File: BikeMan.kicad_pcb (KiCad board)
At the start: 2 copper layers, 152.4 x 127 mm, 86 parts, among them J1 USB_A_stacked, J10 Conn_01x04_Female, J11 Conn_01x04_Female, J12 MagJack, J13 Micro_SD_Card_Det, J14 HDMI_A_1.4, J2 USB_A_stacked, J3 Barrel_Jack, J4 Conn_01x06_Female, J5 Conn_01x06_Female, J6 Conn_01x06_Female, J7 PushConnector_8pos, J8 PushConnector_8pos, J9 PushConnector_8pos, Q1 AUIRF7316QTR, Q2 AUIRF7316QTR, Q3 AUIRF7316QTR, Q4 AUIRF7316QTR, Q5 DMN62D0U-7, Q6 DMN62D0U-7, U1 RT9742GGJ5, U2 TUSB2046IBVF, U3 AP64501, U4 MCP2515, U5 MCP2551, U6 NPIC6C596ADJ, U7 PCF8574DWR, U8 PCF85063A

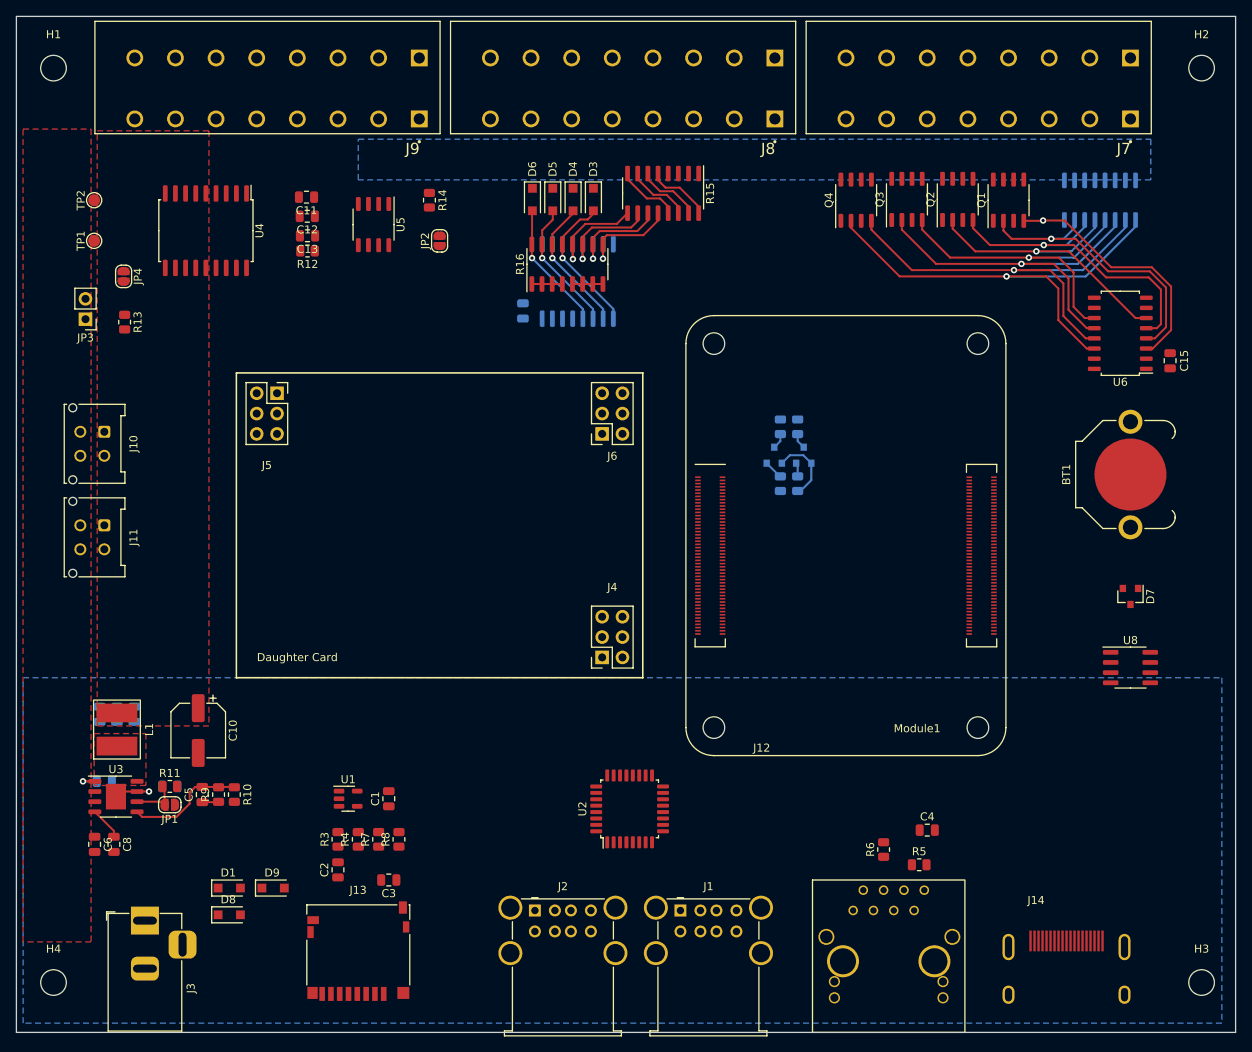
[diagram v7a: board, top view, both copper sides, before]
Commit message: Routing for HDMI, Ethernet, SD Card, CAN
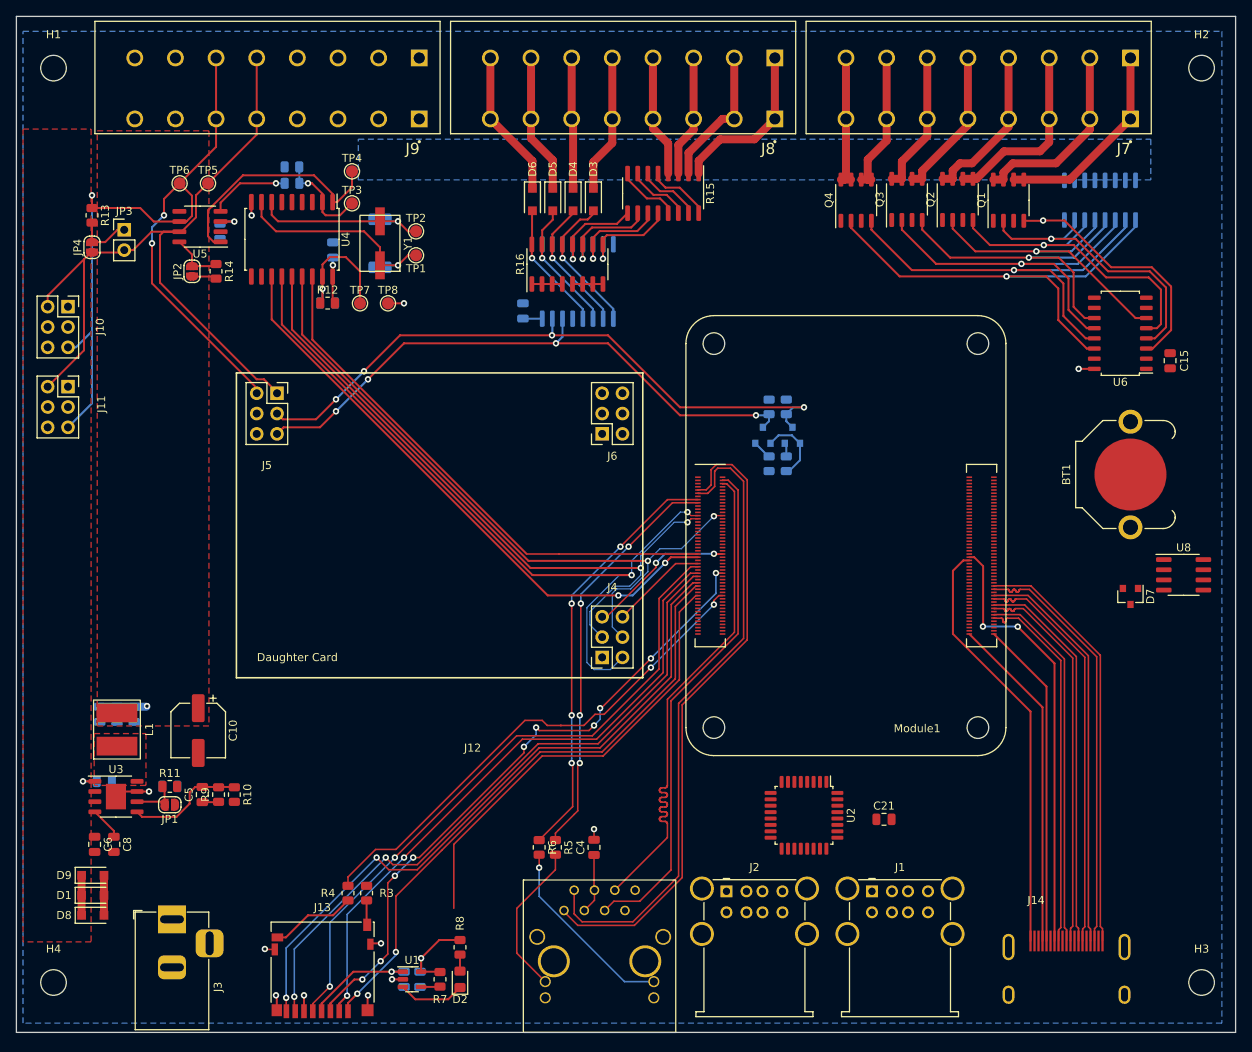
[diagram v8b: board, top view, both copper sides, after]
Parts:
- removed C3: C, Capacitor_SMD:C_0805_2012Metric
- added C19: C, Capacitor_SMD:C_0805_2012Metric, B.Cu at (94.6, 60.8)
- added C20: C, Capacitor_SMD:C_0805_2012Metric, B.Cu at (80.5, 58.5)
- added C21: 0.1uF, Capacitor_SMD:C_0805_2012Metric, F.Cu at (163.5, 132.0)
- added D2: LED_Red, LED_SMD:LED_0805_2012Metric_Pad1.15x1.40mm_HandSolder, F.Cu at (110.5, 152.0)
- added R20: 10k, Resistor_SMD:R_0805_2012Metric, B.Cu at (89.5, 52.5)
- added R21: 22k, Resistor_SMD:R_0805_2012Metric, B.Cu at (89.5, 50.4)
- added TP3: TestPoint, TestPoint:TestPoint_Pad_D1.5mm, F.Cu at (97.0, 55.0)
- added TP4: TestPoint, TestPoint:TestPoint_Pad_D1.5mm, F.Cu at (97.0, 51.0)
- added TP5: TestPoint, TestPoint:TestPoint_Pad_D1.5mm, F.Cu at (79.0, 52.5)
- added TP6: TestPoint, TestPoint:TestPoint_Pad_D1.5mm, F.Cu at (75.5, 52.5)
- added TP7: TestPoint, TestPoint:TestPoint_Pad_D1.5mm, F.Cu at (98.0, 67.5)
- added TP8: TestPoint, TestPoint:TestPoint_Pad_D1.5mm, F.Cu at (101.5, 67.5)
- added Y1: ABLS7M-16.000MHZ-B-2-T, footprints:Crystal-ABLS7M, F.Cu at (100.5, 60.0)
- C1, C11, C12, C13, C2: moved to B.Cu
- J10, J11: value Conn_01x04_Female -> Conn_01x06_Male; footprint Connector_Molex:Molex_Micro-Fit_3.0_43045-0412_2x02_P3.00mm_Vertical -> Connector_PinSocket_2.54mm:PinSocket_2x03_P2.54mm_Vertical
- moved R5 45.5 mm to (122.4, 135.5), turned to -90 degrees
- moved R6 43.1 mm to (120.4, 135.5), turned to -90 degrees
- moved C4 41.7 mm to (127.3, 135.5), turned to 90 degrees
- moved TP2 40.4 mm to (105.0, 58.5), turned to 0 degrees
- moved TP1 40.3 mm to (105.0, 61.5), turned to 0 degrees
- moved J12 36.1 mm to (123.5, 143.4)
- moved JP2 31.2 mm to (77.0, 63.5)
- moved R14 28.1 mm to (80.0, 63.5)
- moved J2 24.1 mm to (143.8, 141.0)
- moved J1 24.1 mm to (162.0, 141.0)
- moved U1 23.9 mm to (104.5, 152.0)
- moved C1 22.9 mm to (105.5, 152.0), turned to -90 degrees
- moved D9 22.6 mm to (64.6, 139.0)
- moved U2 21.8 mm to (153.5, 131.5), turned to -90 degrees
- moved U5 21.7 mm to (78.0, 57.9), turned to 180 degrees
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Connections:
- net /ComputeModule_A/Eth_Rx_{+} renamed /ComputeModule_A/Eth_Rx+
- net /ComputeModule_A/Eth_Rx_{-} renamed /ComputeModule_A/Eth_Rx-
- net /ComputeModule_A/Eth_Tx_{+} renamed /ComputeModule_A/Eth_Tx+
- net /ComputeModule_A/Eth_Tx_{-} renamed /ComputeModule_A/Eth_Tx-
- H1 pad 1: no_connect_209 -> no_connect_211
- H2 pad 1: no_connect_210 -> no_connect_212
- H3 pad 1: no_connect_211 -> no_connect_213
- H4 pad 1: no_connect_212 -> no_connect_214
- J1 pad 3: /D_{2}+ -> /D_{2}-
- J1 pad 6: /D_{1}+ -> /D_{1}-
- J10 pad 3: /CAN_{L} -> +12V
- J11 pad 3: /CAN_{L} -> +12V
- J12 pad 1: no_connect_213 -> no_connect_215
- J12 pad 8: no_connect_215 -> no_connect_217
- J13 pad 4: /ComputeModule_A/SD.power -> /ComputeModule_A/SD.POWER
- J2 pad 2: /D_{4}+ -> /D_{4}-
- J2 pad 6: /D_{3}+ -> /D_{3}-
- J4 pad 2: /CAN_{H} -> /SPI.CLK
- J4 pad 3: /CAN_{L} -> /SPI.MOSI
- J4 pad 4: /SDA_{5V} -> /SPI.MISO
- J4 pad 5: /SCL_{5V} -> /SPI.~CS_{ES1}
- J4 pad 6: GND -> /~INT_{ES1}
- J5 pad 1: +12V -> /CAN_{H}
- J5 pad 2: /SPI.MISO -> /CAN_{L}
- J5 pad 3: /SPI.MOSI -> /SDA_{5V}
- J5 pad 4: /SPI.CLK -> +12V
- J5 pad 5: /SPI.~CS_{ES1} -> /SCL_{5V}
- J5 pad 6: /~INT_{ES1} -> GND
- J9 pad 1: +12V -> GND
- J9 pad 2: +12V -> GND
- J9 pad 3: /CAN_{H} -> GND
- J9 pad 4: /CAN_{L} -> GND
- J9 pad 5: GND -> /CAN_{H}
- J9 pad 6: GND -> /CAN_{L}
- J9 pad 7: GND -> +12V
- J9 pad 8: GND -> +12V
- Module1 pad 10: no_connect_216 -> no_connect_218
- Module1 pad 102: no_connect_217 -> no_connect_219
- Module1 pad 104: no_connect_218 -> no_connect_220
- Module1 pad 106: no_connect_219 -> no_connect_221
- Module1 pad 109: no_connect_220 -> no_connect_222
- Module1 pad 110: no_connect_221 -> no_connect_223
- Module1 pad 111: no_connect_222 -> no_connect_224
- Module1 pad 112: no_connect_223 -> no_connect_225
- Module1 pad 115: no_connect_224 -> no_connect_226
- Module1 pad 116: no_connect_225 -> no_connect_227
- Module1 pad 117: no_connect_226 -> no_connect_228
- Module1 pad 118: no_connect_227 -> no_connect_229
- Module1 pad 12: no_connect_228 -> no_connect_230
- Module1 pad 121: no_connect_229 -> no_connect_231
- Module1 pad 122: no_connect_230 -> no_connect_232
- Module1 pad 123: no_connect_231 -> no_connect_233
- Module1 pad 124: no_connect_232 -> no_connect_234
- Module1 pad 127: no_connect_233 -> no_connect_235
- Module1 pad 128: no_connect_234 -> no_connect_236
- Module1 pad 129: no_connect_235 -> no_connect_237
- Module1 pad 130: no_connect_236 -> no_connect_238
- Module1 pad 133: no_connect_237 -> no_connect_239
- Module1 pad 134: no_connect_238 -> no_connect_240
- Module1 pad 135: no_connect_239 -> no_connect_241
- Module1 pad 136: no_connect_240 -> no_connect_242
- Module1 pad 139: no_connect_241 -> no_connect_243
- Module1 pad 140: no_connect_242 -> no_connect_244
- Module1 pad 141: no_connect_243 -> no_connect_245
- Module1 pad 142: no_connect_244 -> no_connect_246
- Module1 pad 143: no_connect_245 -> no_connect_247
- Module1 pad 145: no_connect_246 -> no_connect_248
- Module1 pad 146: no_connect_247 -> no_connect_249
- Module1 pad 147: no_connect_248 -> no_connect_250
- Module1 pad 148: no_connect_249 -> no_connect_251
- Module1 pad 149: no_connect_250 -> no_connect_252
- Module1 pad 152: no_connect_251 -> no_connect_253
- Module1 pad 154: no_connect_252 -> no_connect_254
- Module1 pad 157: no_connect_253 -> no_connect_255
- Module1 pad 158: no_connect_254 -> no_connect_256
- Module1 pad 159: no_connect_255 -> no_connect_257
- Module1 pad 160: no_connect_256 -> no_connect_258
- Module1 pad 163: no_connect_257 -> no_connect_259
- Module1 pad 164: no_connect_258 -> no_connect_260
- Module1 pad 165: no_connect_259 -> no_connect_261
- Module1 pad 166: no_connect_260 -> no_connect_262
- Module1 pad 169: no_connect_261 -> no_connect_263
- Module1 pad 171: no_connect_262 -> no_connect_264
- Module1 pad 175: no_connect_263 -> no_connect_265
- Module1 pad 177: no_connect_264 -> no_connect_266
- Module1 pad 181: no_connect_265 -> no_connect_267
- Module1 pad 183: no_connect_266 -> no_connect_268
- Module1 pad 187: no_connect_267 -> no_connect_269
- Module1 pad 189: no_connect_268 -> no_connect_270
- Module1 pad 19: no_connect_269 -> no_connect_271
- Module1 pad 193: no_connect_270 -> no_connect_272
- Module1 pad 195: no_connect_271 -> no_connect_273
- Module1 pad 25: /~GPIO_{OE} -> /SPI.CLK
- Module1 pad 26: Net-(Module1-Pad26) -> /SPI.MISO
- Module1 pad 27: /~GPIO_{RS} -> /SPI.MOSI
- Module1 pad 29: /GPIO_{rCLK} -> Net-(Module1-Pad29)
- Module1 pad 3: no_connect_272 -> no_connect_274
- Module1 pad 31: /GPIO_{sCLK} -> Net-(Module1-Pad31)
- Module1 pad 37: /GPIO_{DATA} -> Net-(Module1-Pad37)
- Module1 pad 39: /SPI.CLK -> Net-(Module1-Pad39)
- Module1 pad 41: /SPI.MOSI -> Net-(Module1-Pad41)
- Module1 pad 45: /SPI.MISO -> Net-(Module1-Pad45)
- Module1 pad 47: /SPI.~CS_{CAN} -> Net-(Module1-Pad47)
- Module1 pad 49: /~INT_{CAN} -> /SPI.~CS_{CAN}
- Module1 pad 5: no_connect_273 -> no_connect_275
- Module1 pad 50: Net-(Module1-Pad50) -> /SPI.~CS_{ES1}
- Module1 pad 51: Net-(Module1-Pad51) -> /~INT_{CAN}
- Module1 pad 55: Net-(Module1-Pad55) -> /~INT_{ES1}
- R3 pad 2: /ComputeModule_A/SD_Detect_{A} -> /ComputeModule_A/SD.Detect_{A}
- R4 pad 2: /ComputeModule_A/SD_Detect_{B} -> /ComputeModule_A/SD.Detect_{B}
- U2 pad 26: Net-(U2-Pad26) -> +3V3
- U2 pad 5: Net-(U2-Pad5) -> no_connect_276
- U2 pad 8: Net-(U2-Pad8) -> +3V3
- U4 pad 10: no_connect_274 -> no_connect_277
- U4 pad 11: no_connect_275 -> no_connect_278
- U4 pad 2: /CAN Peripherals/CAN_{Rx} -> /CAN Peripherals/CAN_{RxLOW}
- U4 pad 3: no_connect_276 -> no_connect_279
- U4 pad 4: no_connect_277 -> no_connect_280
- U4 pad 5: no_connect_278 -> no_connect_281
- U4 pad 6: no_connect_279 -> no_connect_282
- U5 pad 5: no_connect_280 -> no_connect_283
- U6 pad 9: no_connect_281 -> no_connect_284
- U8 pad 3: no_connect_282 -> no_connect_285
- U8 pad 7: no_connect_283 -> no_connect_286
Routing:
- net /CAN_{L}: track 0.00 -> 104.6 mm, vias 0 -> 3
- net /SPI.CLK: track 0.00 -> 95.0 mm, vias 0 -> 2
- net /CAN_{H}: track 0.00 -> 93.8 mm
- net /SPI.MISO: track 0.00 -> 86.8 mm, vias 0 -> 2
- net /SPI.MOSI: track 0.00 -> 86.1 mm, vias 0 -> 2
- net /ComputeModule_A/SD.DAT1: track 0.00 -> 84.8 mm, vias 0 -> 2
- net /ComputeModule_A/SD.DAT0: track 0.00 -> 83.6 mm, vias 0 -> 2
- net /ComputeModule_A/SD.CLK: track 0.00 -> 81.6 mm, vias 0 -> 2
- net /ComputeModule_A/SD.CMD: track 0.00 -> 81.1 mm, vias 0 -> 10
- net /ComputeModule_A/Eth_Rx+: track 0.00 -> 80.6 mm
- net /ComputeModule_A/Eth_Rx-: track 0.00 -> 80.3 mm
- net /ComputeModule_A/SD.DAT3: track 0.00 -> 79.3 mm, vias 0 -> 2
- net /SDA_{5V}: track 1.96 -> 80.9 mm, vias 0 -> 4
- net /ComputeModule_A/SD.DAT2: track 0.00 -> 76.0 mm, vias 0 -> 2
- net /~INT_{CAN}: track 0.00 -> 74.9 mm, vias 0 -> 2
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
